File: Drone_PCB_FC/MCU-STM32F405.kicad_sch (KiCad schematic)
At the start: 14 parts, among them U4 STM32F405RGTx, Y1 Crystal_GND24

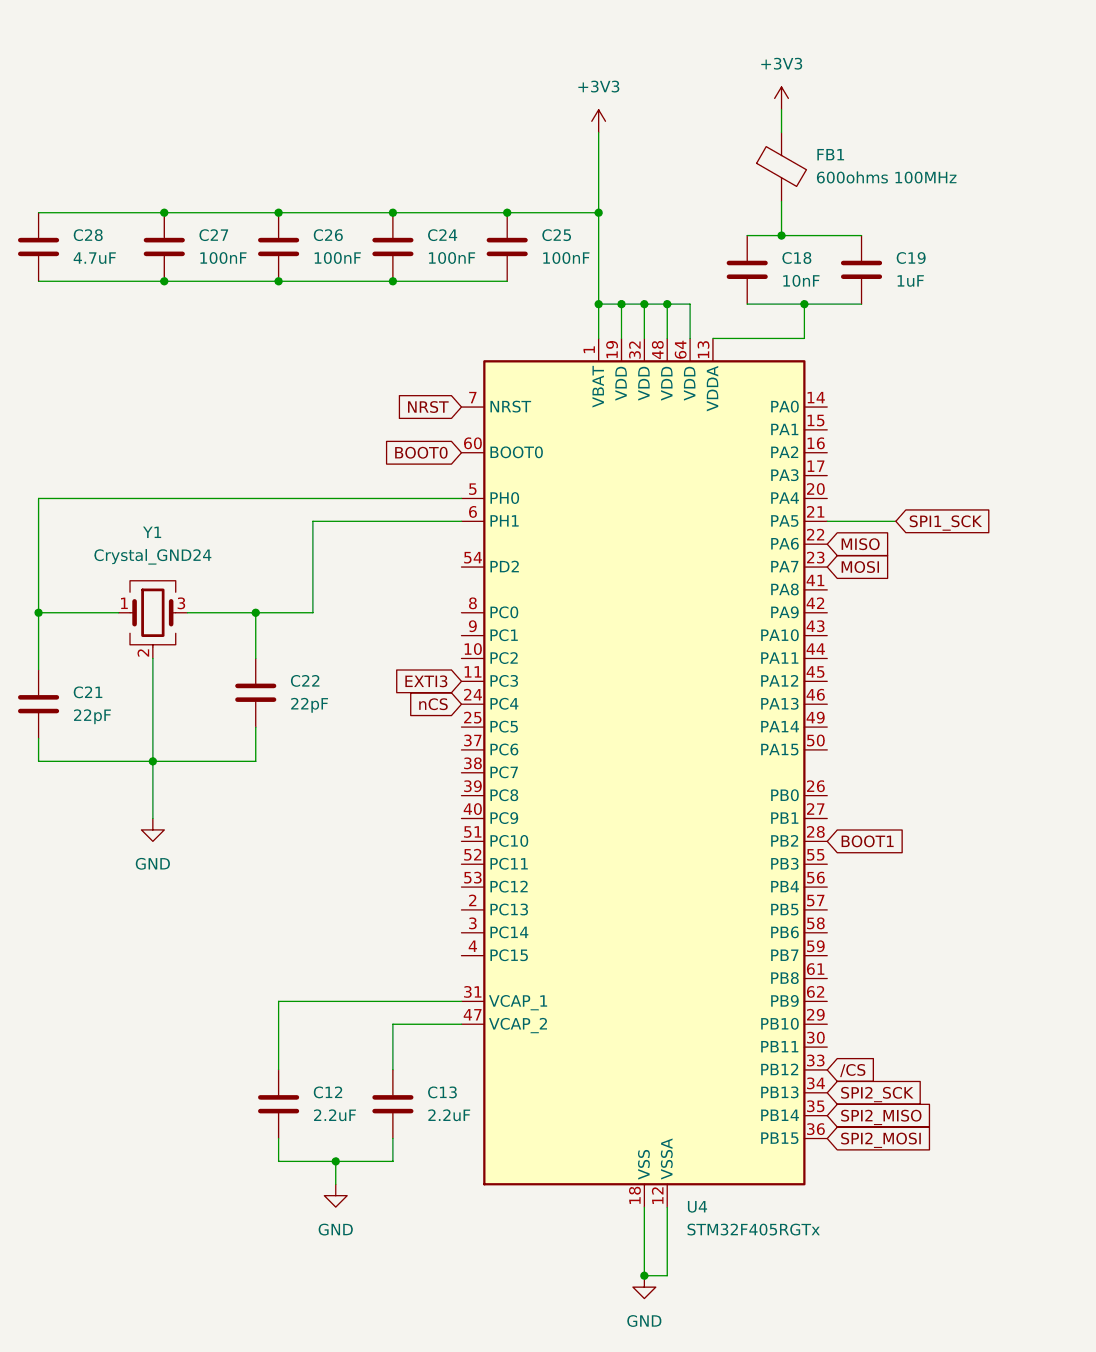
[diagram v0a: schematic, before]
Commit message: almost done with the schmatic design
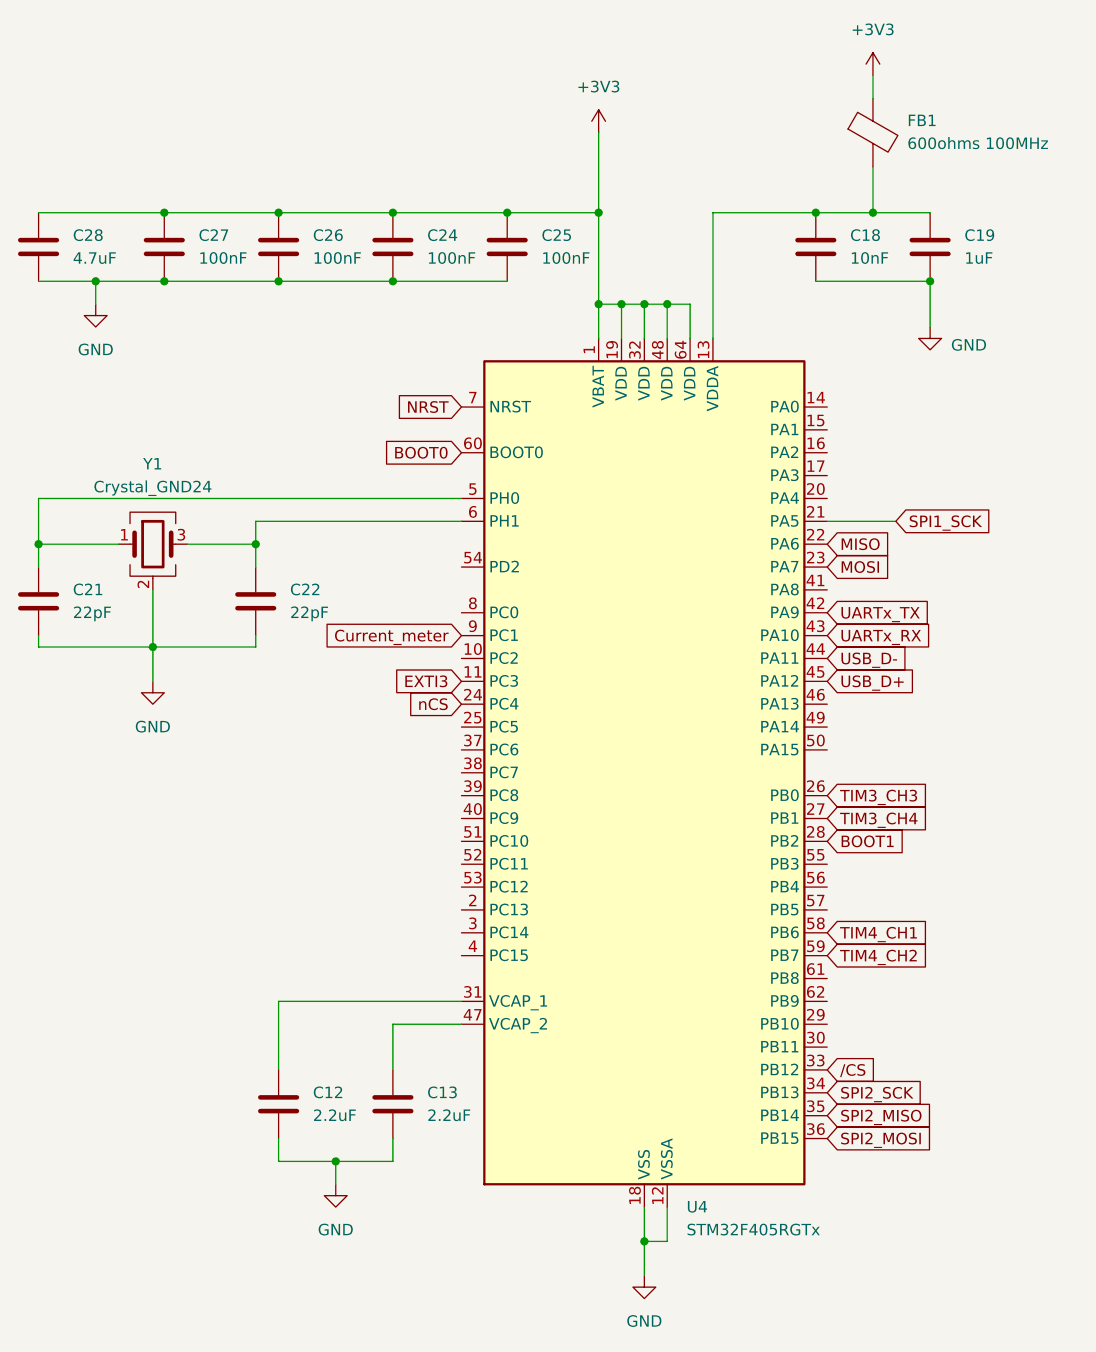
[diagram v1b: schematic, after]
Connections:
- net GND: now also C18.2, C19.2, C24.2, C25.2, C26.2, C27.2, C28.2
- net TIM3_CH3: now reaches U4.26 (PB0)
- net TIM3_CH4: now reaches U4.27 (PB1)
- net UARTx_TX: now reaches U4.42 (PA9)
- net UARTx_RX: now reaches U4.43 (PA10)
- net USB_D-: now reaches U4.44 (PA11)
- net USB_D+: now reaches U4.45 (PA12)
- net TIM4_CH1: now reaches U4.58 (PB6)
- net TIM4_CH2: now reaches U4.59 (PB7)
- net Current_meter: now reaches U4.9 (PC1)
- net at C18.1, C19.1, FB1.2: now also U4.13 (VDDA)
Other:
- moved on the sheet: C18, C19, C21, C22, FB1, Y1
